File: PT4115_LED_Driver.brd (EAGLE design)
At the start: 50 x 50 mm, 61 parts, among them IC1 PCA9685PW, IC2 TMP421

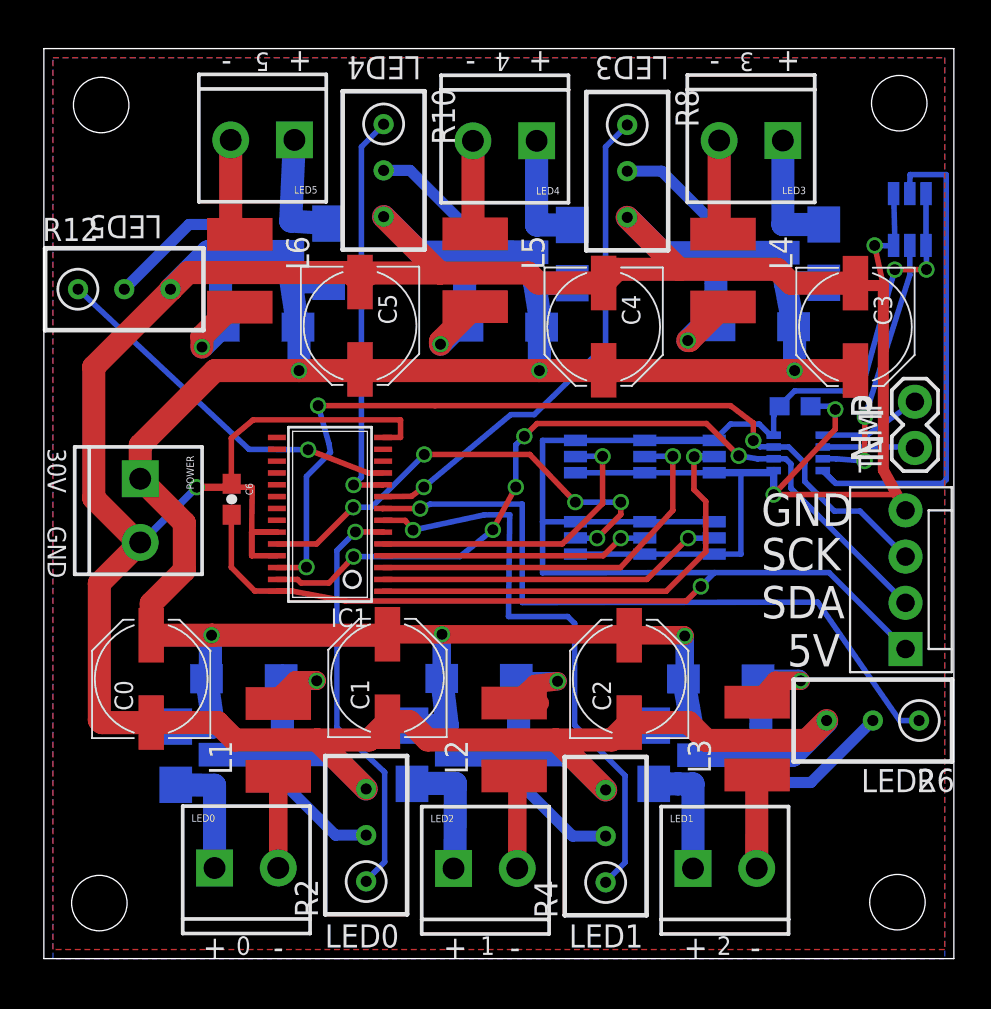
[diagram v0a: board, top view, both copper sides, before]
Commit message: Simplified some routes.  Cleaned up ground and 5v planes.  Added img exports.
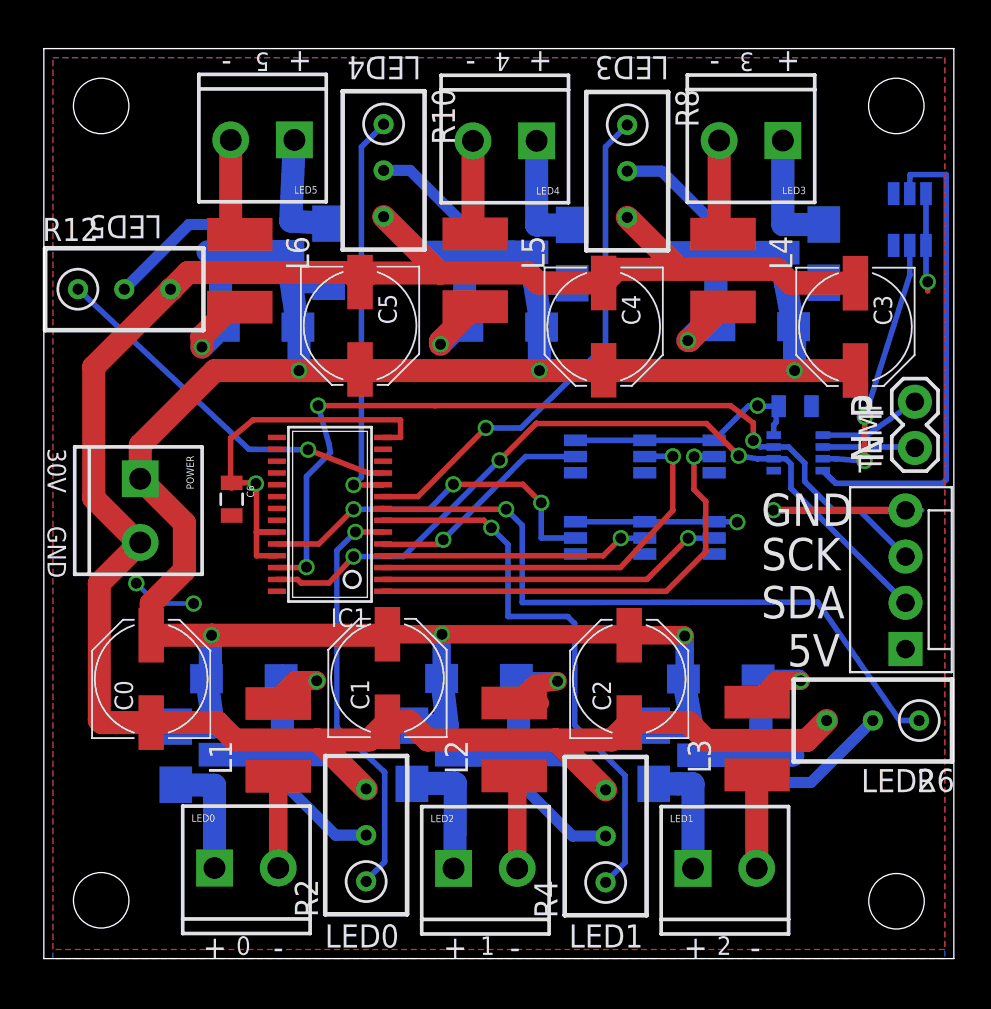
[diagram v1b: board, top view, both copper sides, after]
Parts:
- removed U$1, U$2: (no value), 1dah:STAND-OFF-TIGHT
- added 5V, 5V1: (no value), 1dah:STAND-OFF-TIGHT
- C6, C7: device SparkFun:0603-CAP -> SparkFun:0805
- moved U$4 0.18 mm to (3.15, 3.20)
- moved U$3 0.07 mm to (46.8, 3.15)
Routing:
- net GND: track 283.9 -> 205.7 mm, vias 4 -> 2
- net 5V: track 103.0 -> 33.5 mm, vias 3 -> 5
- net A5: track 25.8 -> 20.1 mm, vias 5 -> 3
- net A4: track 17.1 -> 12.6 mm
- net SDA: track 45.1 -> 43.4 mm, vias 5 -> 3
- net PWM1: track 32.5 -> 31.0 mm
- net PWM2: track 38.4 -> 37.5 mm

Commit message: Added led 5v power indicator
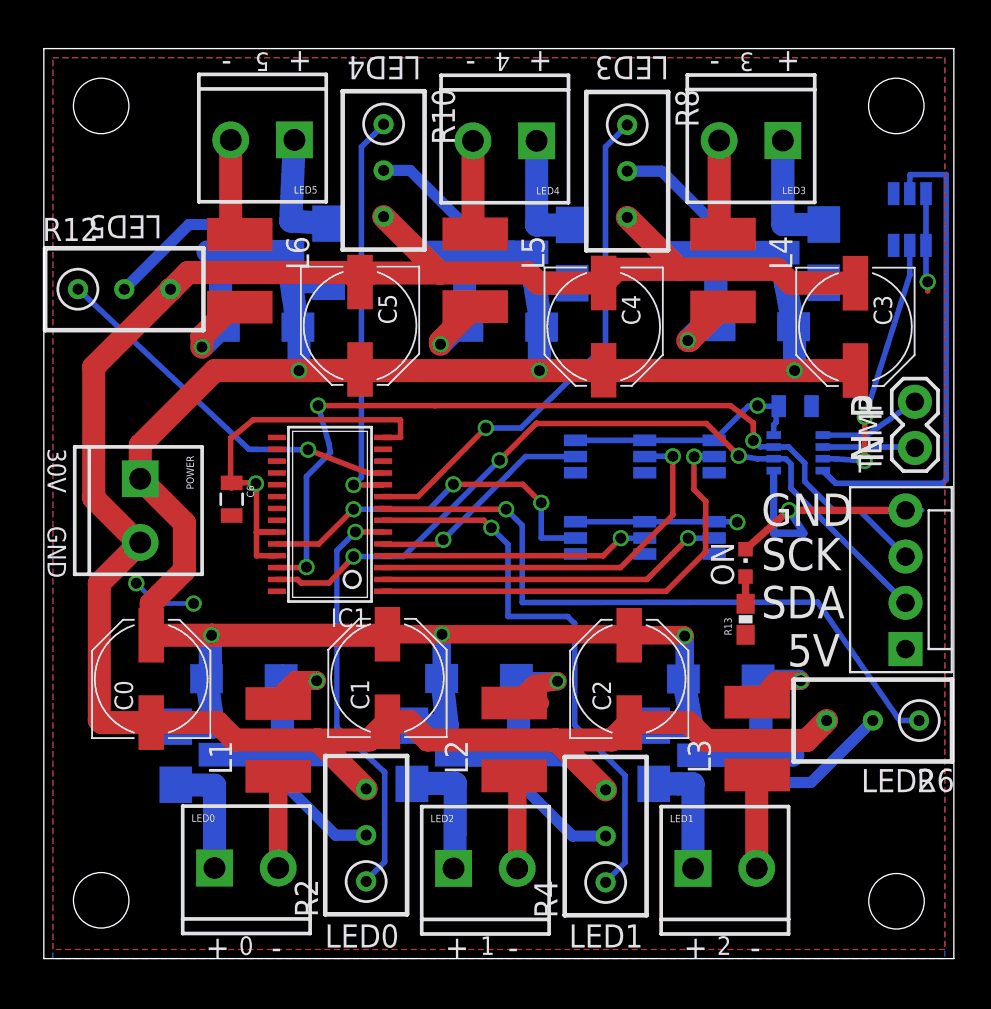
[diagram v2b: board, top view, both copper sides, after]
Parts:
- added ON: GREEN, led:CHIPLED_0603
- added R13: 1k, SparkFun:0603-RES
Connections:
- new net N$30: ON.A, R13.2
- net 5V: now also R13.1
- net GND: now also ON.C
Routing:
- net GND: track 205.7 -> 214.6 mm
- net N$30: track 0.00 -> 1.50 mm
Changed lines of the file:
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@@
 <text x="44.9072" y="9.144" size="1.27" layer="121">LED2</text>
 <text x="15.4432" y="0.6096" size="1.27" layer="121">LED0</text>
-<text x="8.7376" y="0" size="1.27" layer="121">+</text>
-<text x="21.9456" y="0" size="1.27" layer="121">+</text>
+<text x="8.89" y="0" size="1.27" layer="121">+</text>
+<text x="22.0472" y="0" size="1.27" layer="121">+</text>
 <text x="35.1536" y="0" size="1.27" layer="121">+</text>
 <text x="40.2336" y="48.768" size="1.27" layer="121">+</text>
@@
 <text x="36.576" y="48.768" size="1.27" layer="121">-</text>
 <text x="38.8112" y="0" size="1.27" layer="121">-</text>
-<text x="25.6032" y="0" size="1.27" layer="121">-</text>
-<text x="12.5984" y="0" size="1.27" layer="121">-</text>
+<text x="25.5016" y="0" size="1.27" layer="121">-</text>
+<text x="12.4968" y="0" size="1.27" layer="121">-</text>
 <text x="25.6032" y="49.784" size="1.016" layer="121" rot="SR180">4</text>
 <text x="39.0144" y="49.784" size="1.016" layer="121" rot="SR180">3</text>
@@
 <text x="20.7264" y="49.5808" size="1.27" layer="121" rot="SR180">LED4</text>
 <text x="6.5024" y="40.8432" size="1.27" layer="121" rot="SR180">LED5</text>
-<text x="10.5664" y="0.2032" size="1.016" layer="121">0</text>
+<text x="10.7188" y="0.2032" size="1.016" layer="121">0</text>
 <text x="23.9776" y="0.2032" size="1.016" layer="121">1</text>
 <text x="36.9824" y="0.2032" size="1.016" layer="121">2</text>
@@
 <element name="U$4" library="1dah" package="STAND-OFF-TIGHT" value="" x="3.1516" y="3.2024"/>
 <element name="5V1" library="1dah" package="STAND-OFF-TIGHT" value="" x="46.838" y="46.8492"/>
+<element name="R13" library="SparkFun" package="0603-RES" value="1k" x="38.5572" y="18.6436" rot="R90"/>
+<element name="ON" library="led" package="CHIPLED_0603" value="GREEN" x="38.5572" y="21.7424"/>
 </elements>
 <signals>
@@
 <wire x1="11.684" y1="22.1344" x2="11.684" y2="23.4188" width="0.3048" layer="1"/>
 <contactref element="IC2" pad="5"/>
-<wire x1="47.3456" y1="24.6286" x2="40.0812" y2="24.6286" width="0.4064" layer="1"/>
-<wire x1="40.0812" y1="24.6286" x2="40.0812" y2="24.638" width="0.4064" layer="1"/>
-<via x="40.0812" y="24.638" extent="1-16" drill="0.6"/>
+<via x="40.9448" y="24.638" extent="1-16" drill="0.6"/>
 <contactref element="C7" pad="1"/>
+<contactref element="ON" pad="C"/>
+<wire x1="40.0996" y1="26.813" x2="40.0996" y2="23.368" width="0.4064" layer="16"/>
+<wire x1="40.0996" y1="23.368" x2="41.7576" y2="23.368" width="0.4064" layer="16"/>
+<wire x1="41.7576" y1="23.368" x2="40.9448" y2="24.638" width="0.4064" layer="16"/>
+<wire x1="40.9448" y1="24.638" x2="43.1292" y2="24.6286" width="0.4064" layer="1"/>
+<wire x1="43.1292" y1="24.6286" x2="47.3456" y2="24.6286" width="0.4064" layer="1"/>
+<wire x1="38.5572" y1="22.4924" x2="40.894" y2="24.5872" width="0.4064" layer="1"/>
+<wire x1="40.894" y1="24.5872" x2="40.9448" y2="24.638" width="0.4064" layer="1"/>
 </signal>
 <signal name="5V">
@@
 <via x="38.1" y="23.9776" extent="1-16" drill="0.6"/>
 <wire x1="38.1" y1="23.9776" x2="38.1" y2="24.0792" width="0.3048" layer="1"/>
+<contactref element="R13" pad="1"/>
 </signal>
 <signal name="A0">
@@
 <contactref element="IC1" pad="3"/>
 <wire x1="18.6404" y1="21.4844" x2="31.6844" y2="21.4844" width="0.3048" layer="1"/>
-<wire x1="31.6844" y1="21.4844" x2="34.56" y2="24.63" width="0.3048" layer="1"/>
-<wire x1="34.56" y1="24.63" x2="34.56" y2="27.6" width="0.3048" layer="1"/>
+<wire x1="31.6844" y1="21.4844" x2="34.56" y2="24.376" width="0.3048" layer="1"/>
+<wire x1="34.56" y1="24.376" x2="34.56" y2="27.6" width="0.3048" layer="1"/>
 <via x="34.56" y="27.6" extent="1-16" drill="0.6"/>
 <wire x1="34.56" y1="27.6" x2="33.0356" y2="27.6" width="0.3048" layer="16"/>
@@
 <wire x1="47.5488" y1="42.0624" x2="47.5996" y2="43.0784" width="0.3048" layer="16"/>
 </signal>
+<signal name="N$30">
+<contactref element="R13" pad="2"/>
+<contactref element="ON" pad="A"/>
+<wire x1="38.5572" y1="20.9924" x2="38.5572" y2="19.4936" width="0.4064" layer="1"/>
+</signal>
 </signals>

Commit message: Switched to larger Panasinonic F size capacitors for low ESR part availability.
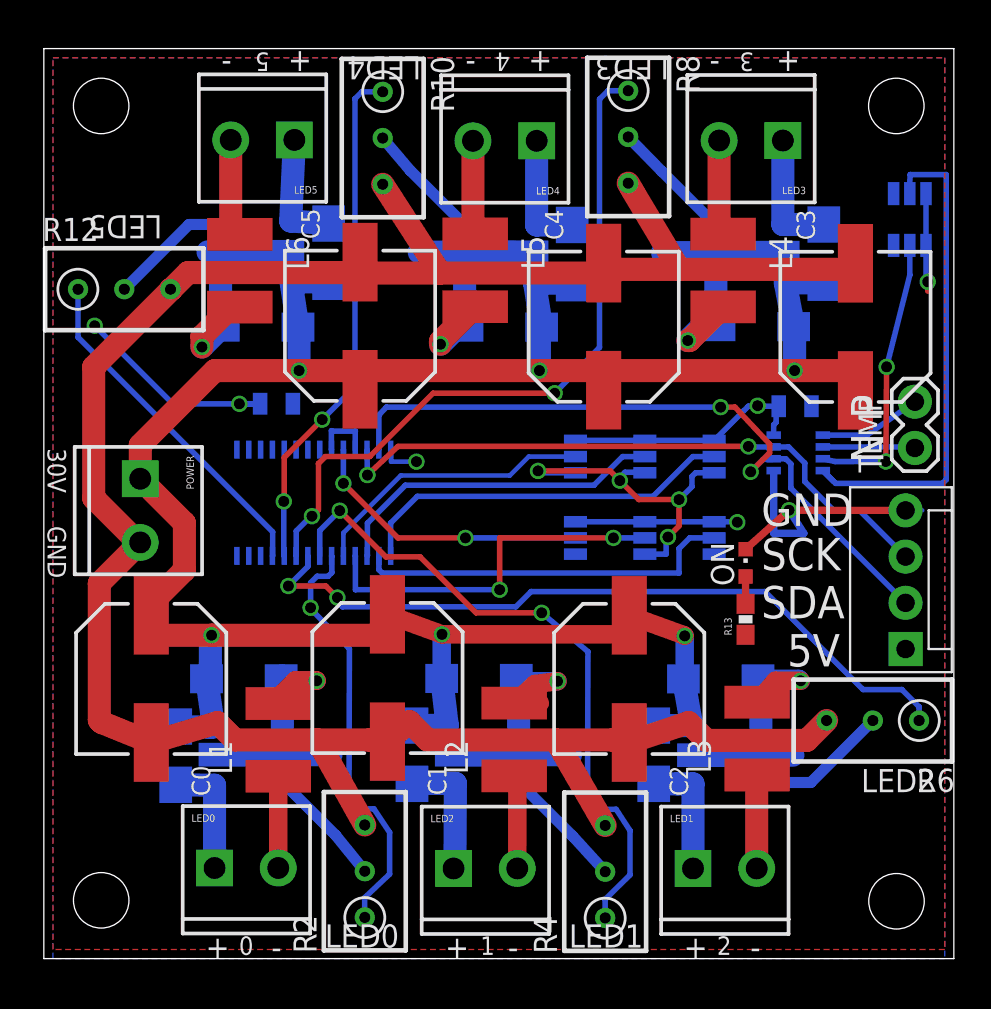
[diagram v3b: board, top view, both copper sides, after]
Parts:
- C0, C1, C2, C3, C4, C5: device SparkFun:PANASONIC_D -> rc-master:CSV-E/F
- moved C6 5.80 mm to (12.8, 30.5), flipped to the bottom, turned to 0 degrees
- moved R2 1.98 mm to (17.6, 4.80)
- moved R4 1.96 mm to (30.8, 4.78)
- moved R8 1.88 mm to (32.1, 45.1)
- moved R10 1.78 mm to (18.6, 45.1)
- moved IC1 1.09 mm to (14.8, 25.0), flipped to the bottom, turned to 0 degrees
- turned C0 to 270 degrees
- turned C1 to 270 degrees
- turned C2 to 270 degrees
- turned C3 to 90 degrees
- turned C4 to 90 degrees
- turned C5 to 90 degrees
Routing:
- net SCK: track 47.9 -> 34.7 mm, vias 3 -> 2
- net PWM3: track 28.2 -> 39.1 mm, vias 1 -> 2
- net 5V: track 33.5 -> 44.1 mm, vias 5 -> 6
- net PWM4: track 22.1 -> 28.4 mm, vias 1 -> 2
- net A3: track 14.8 -> 20.6 mm, vias 1 -> 2
- net PWM1: track 31.0 -> 36.7 mm, vias 1 -> 2
- net VCC: track 129.0 -> 134.5 mm
- net A5: track 20.1 -> 15.8 mm, vias 3 -> 2
- net A0: track 25.2 -> 21.1 mm, vias 1 -> 0
- net SDA: track 43.4 -> 39.3 mm, vias 3 -> 2
- net GND: track 214.6 -> 218.8 mm, vias 2 -> 5
- net PWM2: track 37.5 -> 41.1 mm, vias 1 -> 2
- net A2: track 21.9 -> 18.6 mm, vias 1 -> 0
- net A4: track 12.6 -> 15.8 mm, vias 1 -> 0
- net A1: track 19.1 -> 20.8 mm, vias 1 -> 0
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
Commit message: Switched to larger pad for inductor to source 1.2a part.  Switched top plane from 5V to GND.
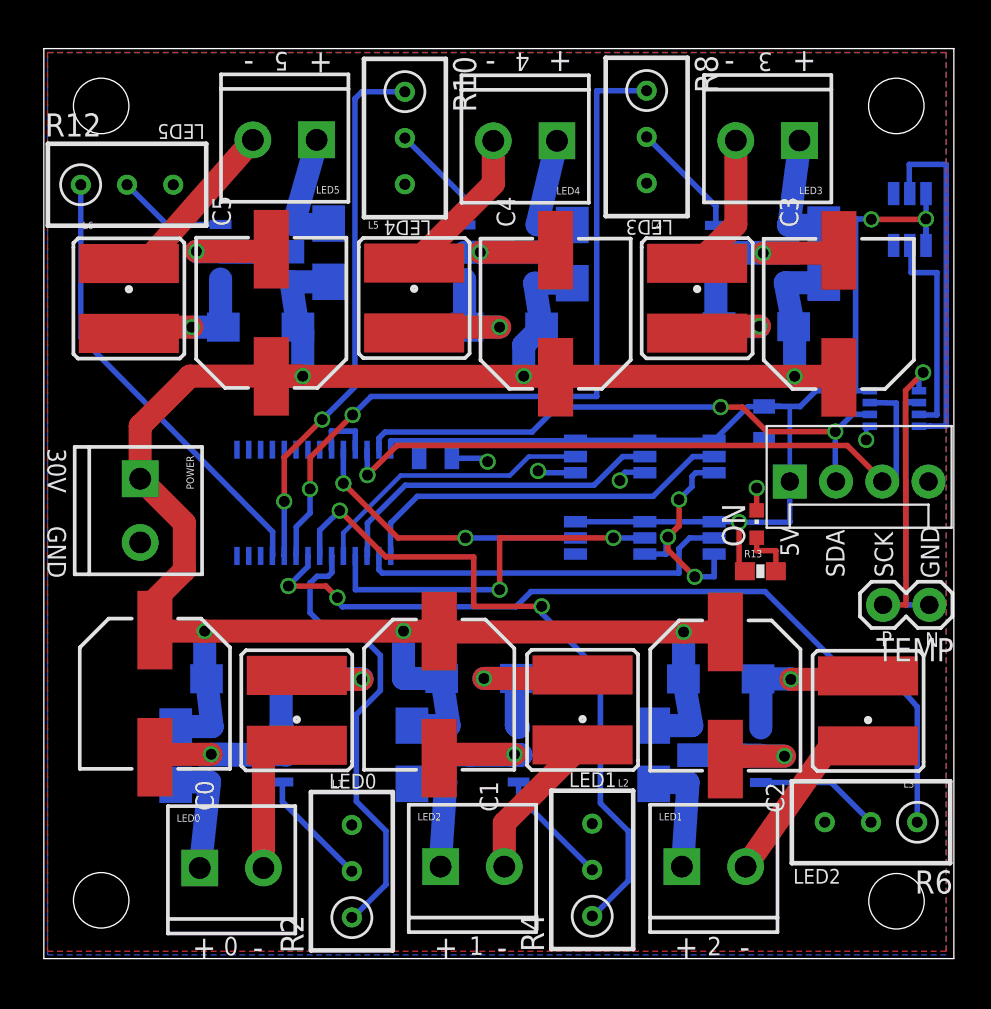
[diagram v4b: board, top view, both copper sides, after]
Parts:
- L1, L2, L3, L4, L5, L6: device rcl:L4532P -> SparkFun:CR54
- moved I2C 11.2 mm to (41.0, 26.2), turned to 0 degrees
- moved C6 9.24 mm to (21.5, 27.5)
- moved TEMP 8.66 mm to (48.7, 19.4), turned to 180 degrees
- moved L6 6.28 mm to (4.67, 36.3), turned to 0 degrees
- moved L3 6.28 mm to (45.3, 13.6), turned to 180 degrees
- moved IC2 5.82 mm to (46.5, 30.3)
- moved R12 5.74 mm to (4.57, 42.5)
- moved R6 5.59 mm to (45.4, 7.49)
- moved C2 5.36 mm to (37.4, 14.5)
- moved C5 4.93 mm to (12.5, 35.5)
- moved L2 4.10 mm to (29.6, 13.7), turned to 180 degrees
- moved L5 3.68 mm to (20.3, 36.3), turned to 0 degrees
- moved C1 2.99 mm to (21.7, 14.5)
- moved R13 2.76 mm to (39.4, 21.3), turned to 0 degrees
- moved C4 2.74 mm to (28.1, 35.4)
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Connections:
- net N$10: now also L1.P$1; no longer L1.1
- net N$11: now also L2.P$1; no longer L2.1
- net N$13: now also L3.P$2; no longer L3.2
- net N$15: now also L3.P$1; no longer L3.1
- net N$17: now also L4.P$2; no longer L4.2
- net N$19: now also L4.P$1; no longer L4.1
- net N$21: now also L5.P$2; no longer L5.2
- net N$23: now also L5.P$1; no longer L5.1
- net N$25: now also L6.P$2; no longer L6.2
- net N$27: now also L6.P$1; no longer L6.1
- net N$4: now also L2.P$2; no longer L2.2
- net N$7: now also L1.P$2; no longer L1.2
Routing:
- net GND: track 218.8 -> 77.3 mm, vias 5 -> 14
- net 5V: track 44.1 -> 69.8 mm, vias 6 -> 3
- net N$2: track 5.64 -> 15.5 mm, vias 0 -> 1
- net N$3: track 5.08 -> 13.9 mm
- net AD0: track 27.8 -> 19.5 mm
- net SDA: track 39.3 -> 32.0 mm
- net PWM5: track 19.1 -> 24.7 mm
- net PWM2: track 41.1 -> 46.6 mm
- net N$15: track 5.14 -> 10.2 mm
- net N$27: track 5.69 -> 9.88 mm
- net N$10: track 5.04 -> 8.57 mm
- net N$23: track 5.16 -> 8.52 mm
- net N$11: track 5.15 -> 8.47 mm
- net AD1: track 15.5 -> 12.2 mm, vias 2 -> 0
- net PWM3: track 39.1 -> 42.4 mm
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- added copper zone on layer 1, net GND
- removed copper zone on layer 1, net 5V

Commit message: Fixed issues with ground pad on TMP421 address jumper.  Moved mounting holes to provide better clearance.  Fixed silkscreen labeling problems with PCA9685 jumper and TMP421 external temp jumper.
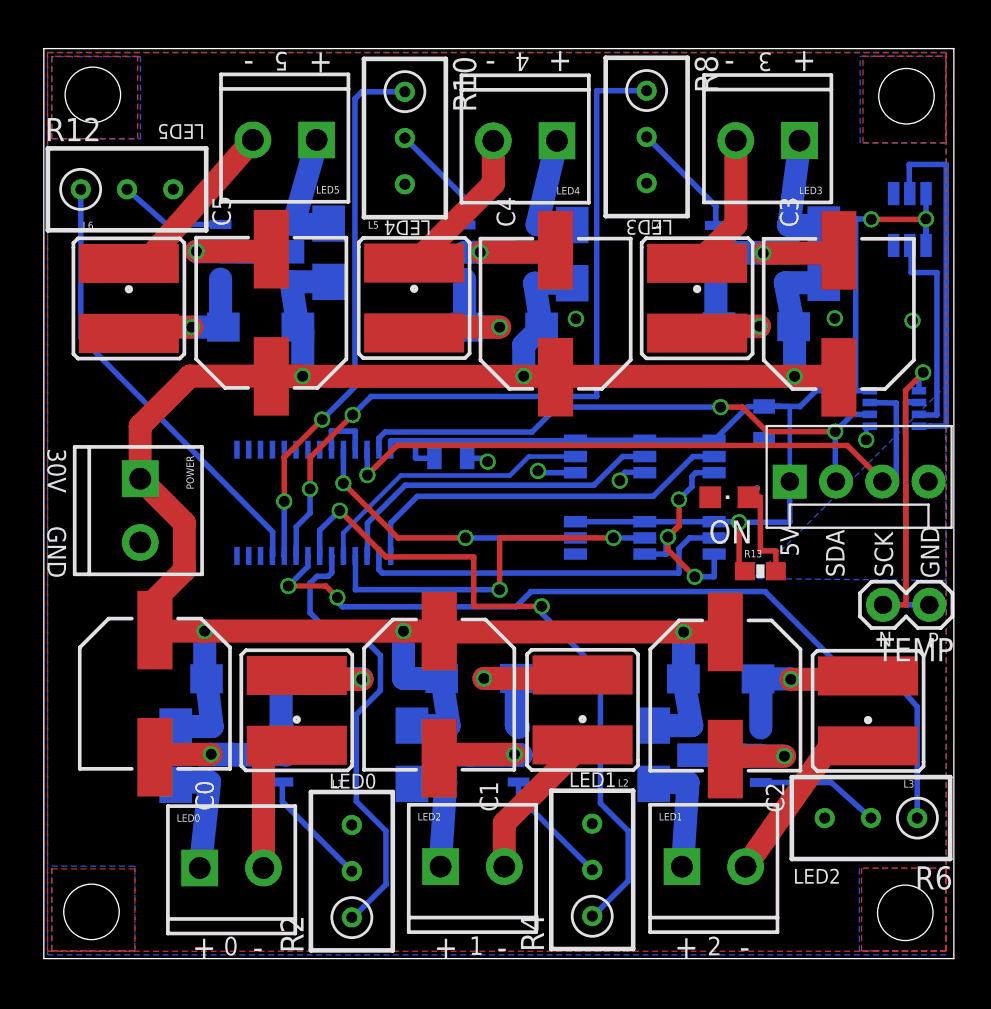
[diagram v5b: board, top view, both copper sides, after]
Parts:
- ON: device led:CHIPLED_0603 -> led:CHIPLED_0805
- moved ON 2.10 mm to (37.7, 25.3), turned to 90 degrees
- moved C6 0.84 mm to (22.4, 27.5)
- moved U$4 0.83 mm to (2.62, 2.57)
- moved U$3 0.80 mm to (47.3, 2.52)
- moved 5V1 0.77 mm to (47.4, 47.4)
- moved 5V 0.76 mm to (2.69, 47.5)
- moved R12 0.25 mm to (4.57, 42.3)
- moved R6 0.23 mm to (45.4, 7.72)
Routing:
- net N$30: track 2.94 -> 5.57 mm
- net GND: track 77.3 -> 75.1 mm, vias 14 -> 16
- net 5V: track 69.8 -> 70.7 mm
- added copper zone on layer 16, net N$37
- added copper zone on layer 16, net N$38
- added copper zone on layer 1, net N$39
- added copper zone on layer 1, net N$40
- added copper zone on layer 1, net N$41
- added copper zone on layer 1, net N$42
- added copper zone on layer 16, net N$43
- added copper zone on layer 16, net N$44
